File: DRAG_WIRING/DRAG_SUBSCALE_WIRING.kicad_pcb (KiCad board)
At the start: 2 copper layers, 80 x 72 mm, 15 parts, among them J1 Conn_01x02, J2 Conn_01x02, J3 Conn_01x02, J4 Conn_01x03, U1 Teensy4.1

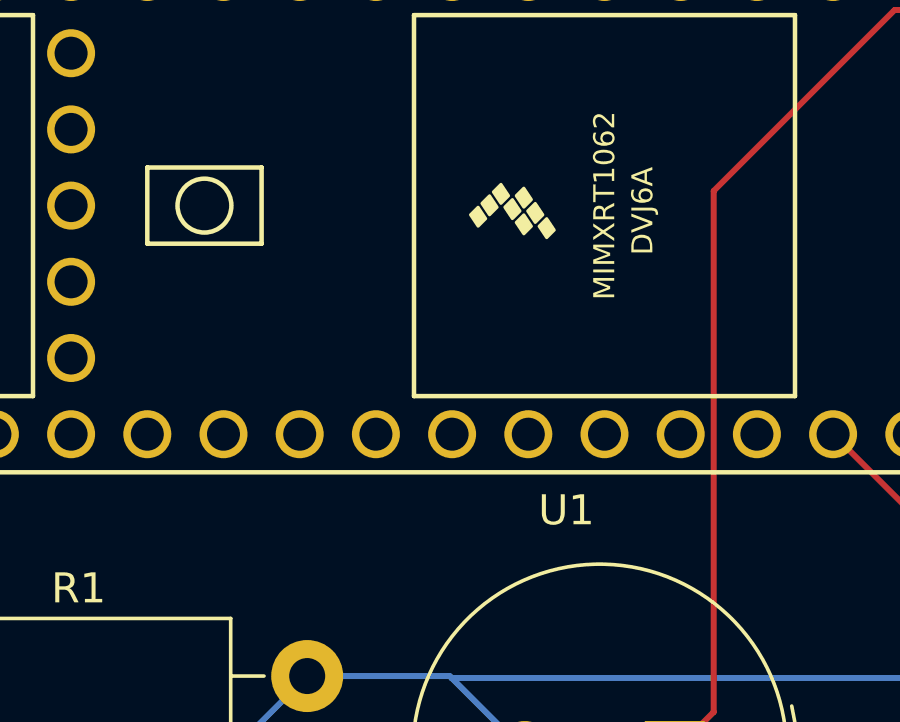
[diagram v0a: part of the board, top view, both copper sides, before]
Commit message: Updating wiring and pcb for servo
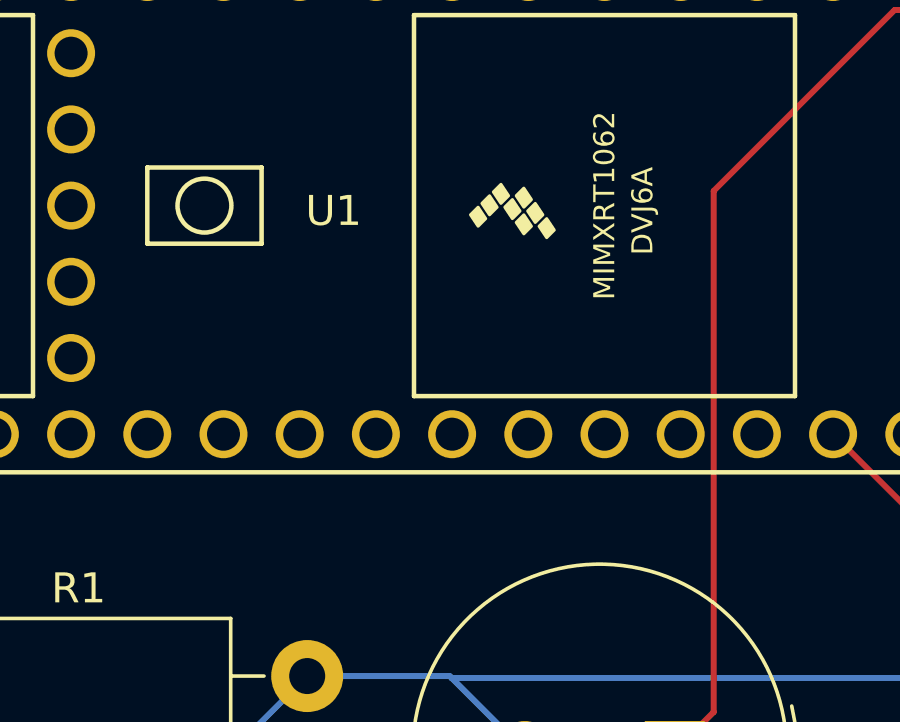
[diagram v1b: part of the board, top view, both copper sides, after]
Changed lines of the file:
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@@
 		(allow_soldermask_bridges_in_footprints no)
 		(pcbplotparams
-			(layerselection 0x00010fc_ffffffff)
-			(plot_on_all_layers_selection 0x0000000_00000000)
+			(layerselection 0x0000020_7ffffffe)
+			(plot_on_all_layers_selection 0x00010a0_80000001)
 			(disableapertmacros no)
 			(usegerberextensions no)
@@
 			(sketchpadsonfab no)
 			(subtractmaskfromsilk no)
-			(outputformat 1)
+			(outputformat 4)
 			(mirror no)
-			(drillshape 1)
+			(drillshape 0)
 			(scaleselection 1)
 			(outputdirectory "")
@@
 		(at 177.26 84.8184 180)
 		(property "Reference" "U1"
-			(at 0 -10.16 0)
+			(at 7.76 -0.1816 0)
 			(layer "F.SilkS")
 			(effects
@@
 		(tags "connector JST XA vertical")
 		(property "Reference" "J2"
-			(at 1.25 -4.4 360)
+			(at 1.25 -4.4 0)
 			(layer "F.SilkS")
 			(effects
@@
 		)
 		(property "Value" "Conn_01x02"
-			(at 1.25 4.4 360)
+			(at 1.25 4.4 0)
 			(layer "F.Fab")
 			(effects
@@
 		)
 		(fp_text user "${REFERENCE}"
-			(at 1.25 1.5 360)
+			(at 1.25 1.5 0)
 			(layer "F.Fab")
 			(effects
@@
 		(tags "connector JST EH vertical")
 		(property "Reference" "J4"
-			(at 2.5 -2.8 360)
+			(at 2.5 -2.8 0)
 			(layer "F.SilkS")
 			(effects
@@
 		)
 		(property "Value" "Conn_01x03"
-			(at 2.5 3.4 360)
+			(at 2.5 3.4 0)
 			(layer "F.Fab")
 			(effects
@@
 		)
 		(fp_text user "${REFERENCE}"
-			(at 2.5 2.31 360)
+			(at 2.5 2.31 0)
 			(layer "F.Fab")
 			(effects

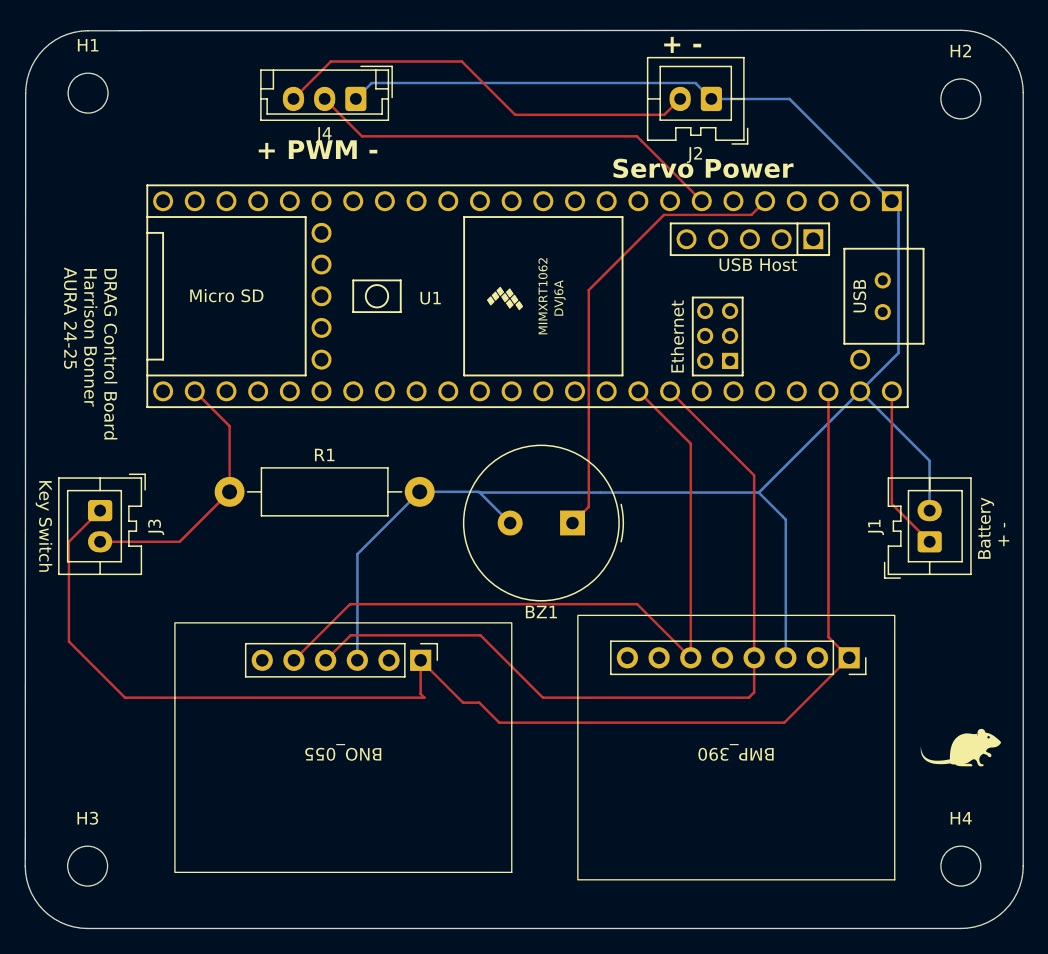
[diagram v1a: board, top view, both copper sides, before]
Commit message: Added more to apogee preditction, adding extra datalog elements, decreased threshold counts
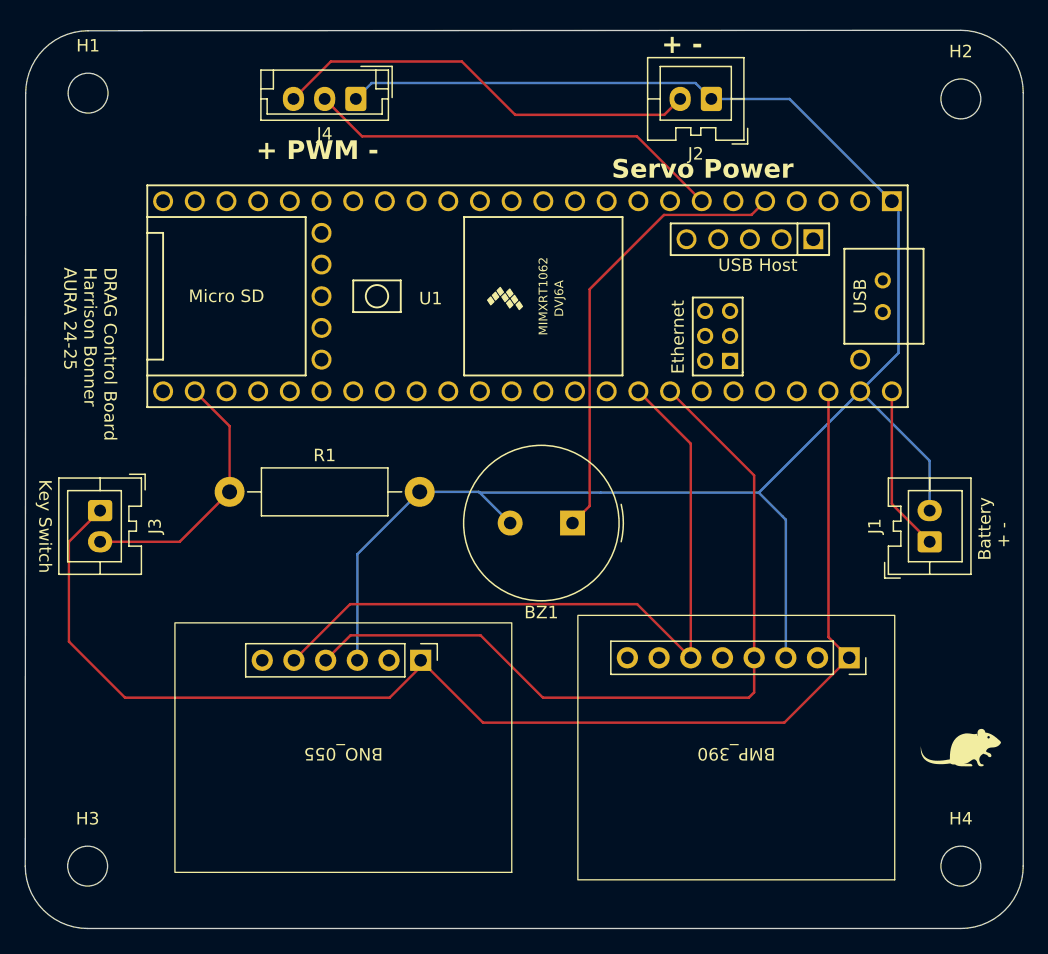
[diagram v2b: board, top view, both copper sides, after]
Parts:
- moved G*** 29.7 mm to (177.2, 116.2)
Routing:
- net 3v3: track 105.6 -> 103.8 mm
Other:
- board text removed: "{dblquote}Thirteen times thirteen passes of the Chaos moon I will give you. Thirteen times thirteen moons I will wait. Go to your legions and your workshops! Bring me victory. Bring me dominance over this mortal realm! You must be as one, work as one, as single-minded as a swarm pouring from a sewer-pipe -- all rats scurry-flood in same direction. Only then will you inherit the ruins of this worl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"
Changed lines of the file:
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@@
 		(allow_soldermask_bridges_in_footprints no)
 		(pcbplotparams
-			(layerselection 0x0000020_7ffffffe)
-			(plot_on_all_layers_selection 0x00010a0_80000001)
+			(layerselection 0x000f0ff_ffffffff)
+			(plot_on_all_layers_selection 0x0001000_00000000)
 			(disableapertmacros no)
 			(usegerberextensions no)
@@
 			(sketchpadsonfab no)
 			(subtractmaskfromsilk no)
-			(outputformat 4)
+			(outputformat 1)
 			(mirror no)
 			(drillshape 0)
 			(scaleselection 1)
-			(outputdirectory "")
+			(outputdirectory "pcbFiles/")
 		)
 	)
@@
 	(footprint "LOGO"
 		(layer "B.Cu")
-		(at 178.5 86.5 180)
+		(at 177.165 116.205 180)
 		(property "Reference" "G***"
 			(at 0 0 0)
@@
 		(layer "Edge.Cuts")
 	)
-	(gr_text "{dblquote}Thirteen times thirteen passes of the Chaos moon I will give you.\n Thirteen times thirteen moons I will wait. \n Go to your legions and your workshops!\n\n Bring me victory.\n Bring me dominance over this mortal realm!\n You must be as one, work as one, \n as single-minded as a swarm pouring from a sewer-pipe\n -- all rats scurry-flood in same direction.\n Only then will you inherit the ruins of this world,\n only then will you rule.\n Thirteen times thirteen moons!\n Fail, and all will suffer the fate of the seer.{dblquote}\n\n-Great Horned Rat\n"
-		(at 201.5 131.5 0)
-		(layer "B.SilkS")
-		(effects
-			(font
-				(size 1 1)
-				(thickness 0.1)
-			)
-			(justify left bottom mirror)
-		)
-	)
 	(gr_text "+ -\n"
 		(at 188 65.5 0)
@@
 	)
 	(segment
-		(start 143 102)
-		(end 140.5 104.5)
-		(width 0.2)
-		(layer "F.Cu")
-		(net 2)
-	)
-	(segment
-		(start 175 119)
-		(end 197.85 119)
-		(width 0.2)
-		(layer "F.Cu")
-		(net 2)
-	)
-	(segment
-		(start 197.85 119)
-		(end 203.05 113.8)
+		(start 168.7 114.51)
+		(end 168.7 114)
 		(width 0.2)
 		(layer "F.Cu")
@@
 	)
 	(segment
-		(start 172.1 117.4)
-		(end 173.4 117.4)
+		(start 168.7 114)
+		(end 173.7 119)
 		(width 0.2)
 		(layer "F.Cu")
@@
 	)
 	(segment
-		(start 201.39 112.14)
-		(end 203.05 113.8)
+		(start 173.7 119)
+		(end 197.85 119)
 		(width 0.2)
 		(layer "F.Cu")
@@
 	)
 	(segment
-		(start 201.39 92.4384)
-		(end 201.39 112.14)
+		(start 140.5 112.5)
+		(end 145 117)
 		(width 0.2)
 		(layer "F.Cu")
@@
 	)
 	(segment
-		(start 145 117)
-		(end 169 117)
+		(start 140.5 104.5)
+		(end 140.5 112.5)
 		(width 0.2)
 		(layer "F.Cu")
@@
 	)
 	(segment
-		(start 168.7 114)
-		(end 172.1 117.4)
+		(start 201.39 112.14)
+		(end 203.05 113.8)
 		(width 0.2)
 		(layer "F.Cu")
@@
 	)
 	(segment
-		(start 173.4 117.4)
-		(end 175 119)
+		(start 201.39 92.4384)
+		(end 201.39 112.14)
 		(width 0.2)
 		(layer "F.Cu")
@@
 	)
 	(segment
-		(start 168.7 116.7)
-		(end 168.7 114)
+		(start 197.85 119)
+		(end 203.05 113.8)
 		(width 0.2)
 		(layer "F.Cu")
@@
 	)
 	(segment
-		(start 169 117)
-		(end 168.7 116.7)
+		(start 145 117)
+		(end 166.21 117)
 		(width 0.2)
 		(layer "F.Cu")
@@
 	)
 	(segment
-		(start 140.5 104.5)
-		(end 140.5 112.5)
+		(start 143 102)
+		(end 140.5 104.5)
 		(width 0.2)
 		(layer "F.Cu")
@@
 	)
 	(segment
-		(start 140.5 112.5)
-		(end 145 117)
+		(start 166.21 117)
+		(end 168.7 114.51)
 		(width 0.2)
 		(layer "F.Cu")
@@
 	)
 	(segment
-		(start 182.17 84.33)
-		(end 188.2016 78.2984)
+		(start 188.2016 78.2984)
+		(end 195.21 78.2984)
 		(width 0.2)
 		(layer "F.Cu")
@@
 	)
 	(segment
-		(start 182.17 101.700785)
-		(end 182.17 84.33)
+		(start 182.245 101.625785)
+		(end 182.245 84.255)
 		(width 0.2)
 		(layer "F.Cu")
@@
 	)
 	(segment
-		(start 188.2016 78.2984)
-		(end 195.21 78.2984)
+		(start 182.245 84.255)
+		(end 188.2016 78.2984)
 		(width 0.2)
 		(layer "F.Cu")
@@
 	(segment
 		(start 180.870785 103)
-		(end 182.17 101.700785)
+		(end 182.245 101.625785)
 		(width 0.2)
 		(layer "F.Cu")
